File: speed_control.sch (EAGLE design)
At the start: 9 parts

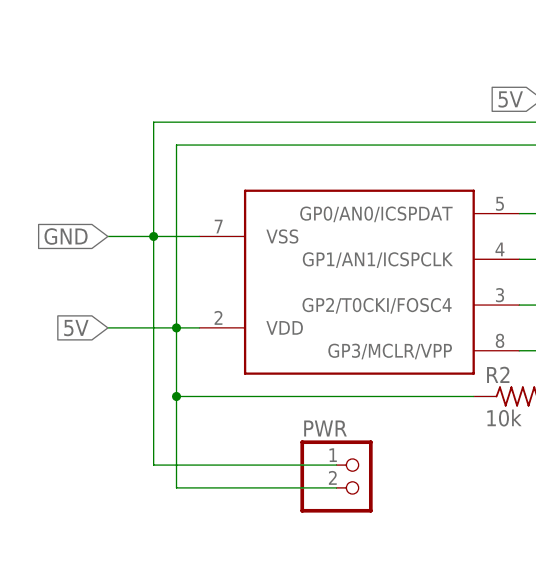
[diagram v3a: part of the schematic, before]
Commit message: Added CAP to circuit
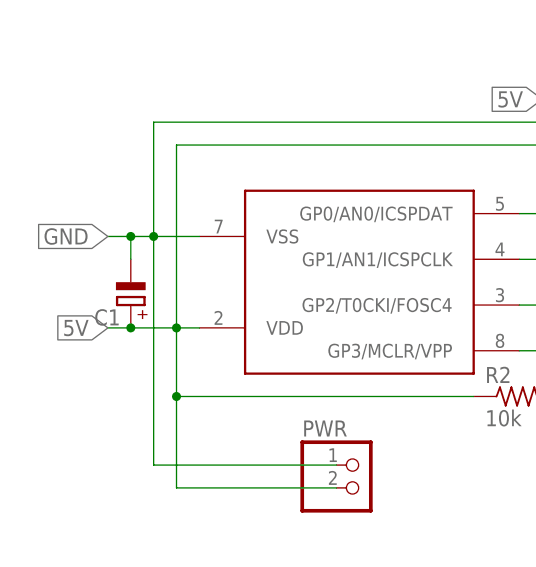
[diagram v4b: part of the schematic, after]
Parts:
- added C1: (no value), rcl:CPOL-EUE3.5-8
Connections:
- net 5V: now also C1.+
- net GND: now also C1.-
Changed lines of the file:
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@@
 <grid distance="0.1" unitdist="inch" unit="inch" style="lines" multiple="1" display="no" altdistance="0.01" altunitdist="inch" altunit="inch"/>
 <layers>
-<layer number="1" name="Top" color="4" fill="1" visible="yes" active="no"/>
-<layer number="2" name="Route2" color="16" fill="1" visible="yes" active="no"/>
-<layer number="3" name="Route3" color="17" fill="1" visible="yes" active="no"/>
-<layer number="4" name="Route4" color="18" fill="1" visible="yes" active="no"/>
-<layer number="5" name="Route5" color="19" fill="1" visible="yes" active="no"/>
-<layer number="6" name="Route6" color="25" fill="1" visible="yes" active="no"/>
-<layer number="7" name="Route7" color="26" fill="1" visible="yes" active="no"/>
-<layer number="8" name="Route8" color="27" fill="1" visible="yes" active="no"/>
-<layer number="9" name="Route9" color="28" fill="1" visible="yes" active="no"/>
-<layer number="10" name="Route10" color="29" fill="1" visible="yes" active="no"/>
-<layer number="11" name="Route11" color="30" fill="1" visible="yes" active="no"/>
-<layer number="12" name="Route12" color="20" fill="1" visible="yes" active="no"/>
-<layer number="13" name="Route13" color="21" fill="1" visible="yes" active="no"/>
-<layer number="14" name="Route14" color="22" fill="1" visible="yes" active="no"/>
-<layer number="15" name="Route15" color="23" fill="1" visible="yes" active="no"/>
-<layer number="16" name="Bottom" color="1" fill="1" visible="yes" active="no"/>
-<layer number="17" name="Pads" color="2" fill="1" visible="yes" active="no"/>
-<layer number="18" name="Vias" color="2" fill="1" visible="yes" active="no"/>
-<layer number="19" name="Unrouted" color="6" fill="1" visible="yes" active="no"/>
-<layer number="20" name="Dimension" color="24" fill="1" visible="yes" active="no"/>
-<layer number="21" name="tPlace" color="7" fill="1" visible="yes" active="no"/>
-<layer number="22" name="bPlace" color="7" fill="1" visible="yes" active="no"/>
-<layer number="23" name="tOrigins" color="15" fill="1" visible="yes" active="no"/>
-<layer number="24" name="bOrigins" color="15" fill="1" visible="yes" active="no"/>
-<layer number="25" name="tNames" color="7" fill="1" visible="yes" active="no"/>
-<layer number="26" name="bNames" color="7" fill="1" visible="yes" active="no"/>
-<layer number="27" name="tValues" color="7" fill="1" visible="yes" active="no"/>
-<layer number="28" name="bValues" color="7" fill="1" visible="yes" active="no"/>
+<layer number="1" name="Top" color="4" fill="1" visible="no" active="no"/>
+<layer number="2" name="Route2" color="16" fill="1" visible="no" active="no"/>
+<layer number="3" name="Route3" color="17" fill="1" visible="no" active="no"/>
+<layer number="4" name="Route4" color="18" fill="1" visible="no" active="no"/>
+<layer number="5" name="Route5" color="19" fill="1" visible="no" active="no"/>
+<layer number="6" name="Route6" color="25" fill="1" visible="no" active="no"/>
+<layer number="7" name="Route7" color="26" fill="1" visible="no" active="no"/>
+<layer number="8" name="Route8" color="27" fill="1" visible="no" active="no"/>
+<layer number="9" name="Route9" color="28" fill="1" visible="no" active="no"/>
+<layer number="10" name="Route10" color="29" fill="1" visible="no" active="no"/>
+<layer number="11" name="Route11" color="30" fill="1" visible="no" active="no"/>
+<layer number="12" name="Route12" color="20" fill="1" visible="no" active="no"/>
+<layer number="13" name="Route13" color="21" fill="1" visible="no" active="no"/>
+<layer number="14" name="Route14" color="22" fill="1" visible="no" active="no"/>
+<layer number="15" name="Route15" color="23" fill="1" visible="no" active="no"/>
+<layer number="16" name="Bottom" color="1" fill="1" visible="no" active="no"/>
+<layer number="17" name="Pads" color="2" fill="1" visible="no" active="no"/>
+<layer number="18" name="Vias" color="2" fill="1" visible="no" active="no"/>
+<layer number="19" name="Unrouted" color="6" fill="1" visible="no" active="no"/>
+<layer number="20" name="Dimension" color="24" fill="1" visible="no" active="no"/>
+<layer number="21" name="tPlace" color="7" fill="1" visible="no" active="no"/>
+<layer number="22" name="bPlace" color="7" fill="1" visible="no" active="no"/>
+<layer number="23" name="tOrigins" color="15" fill="1" visible="no" active="no"/>
+<layer number="24" name="bOrigins" color="15" fill="1" visible="no" active="no"/>
+<layer number="25" name="tNames" color="7" fill="1" visible="no" active="no"/>
+<layer number="26" name="bNames" color="7" fill="1" visible="no" active="no"/>
+<layer number="27" name="tValues" color="7" fill="1" visible="no" active="no"/>
+<layer number="28" name="bValues" color="7" fill="1" visible="no" active="no"/>
 <layer number="29" name="tStop" color="7" fill="3" visible="no" active="no"/>
 <layer number="30" name="bStop" color="7" fill="6" visible="no" active="no"/>
@@
 <layer number="35" name="tGlue" color="7" fill="4" visible="no" active="no"/>
 <layer number="36" name="bGlue" color="7" fill="5" visible="no" active="no"/>
-<layer number="37" name="tTest" color="7" fill="1" visible="yes" active="no"/>
-<layer number="38" name="bTest" color="7" fill="1" visible="yes" active="no"/>
+<layer number="37" name="tTest" color="7" fill="1" visible="no" active="no"/>
+<layer number="38" name="bTest" color="7" fill="1" visible="no" active="no"/>
 <layer number="39" name="tKeepout" color="4" fill="11" visible="no" active="no"/>
 <layer number="40" name="bKeepout" color="1" fill="11" visible="no" active="no"/>
@@
 <layer number="44" name="Drills" color="7" fill="1" visible="no" active="no"/>
 <layer number="45" name="Holes" color="7" fill="1" visible="no" active="no"/>
-<layer number="46" name="Milling" color="3" fill="1" visible="yes" active="no"/>
-<layer number="47" name="Measures" color="7" fill="1" visible="yes" active="no"/>
-<layer number="48" name="Document" color="7" fill="1" visible="yes" active="no"/>
-<layer number="49" name="Reference" color="7" fill="1" visible="yes" active="no"/>
-<layer number="51" name="tDocu" color="7" fill="1" visible="yes" active="no"/>
-<layer number="52" name="bDocu" color="7" fill="1" visible="yes" active="no"/>
+<layer number="46" name="Milling" color="3" fill="1" visible="no" active="no"/>
+<layer number="47" name="Measures" color="7" fill="1" visible="no" active="no"/>
+<layer number="48" name="Document" color="7" fill="1" visible="no" active="no"/>
+<layer number="49" name="Reference" color="7" fill="1" visible="no" active="no"/>
+<layer number="51" name="tDocu" color="7" fill="1" visible="no" active="no"/>
+<layer number="52" name="bDocu" color="7" fill="1" visible="no" active="no"/>
 <layer number="88" name="SimResults" color="9" fill="1" visible="yes" active="yes"/>
 <layer number="89" name="SimProbes" color="9" fill="1" visible="yes" active="yes"/>
@@
 <part name="R3" library="rcl" library_urn="urn:adsk.eagle:library:334" deviceset="R-US_" device="0207/10" package3d_urn="urn:adsk.eagle:package:23491/2" value="1k"/>
 <part name="POT" library="pinhead" library_urn="urn:adsk.eagle:library:325" deviceset="PINHD-1X3" device="" package3d_urn="urn:adsk.eagle:package:22458/2"/>
+<part name="C1" library="rcl" library_urn="urn:adsk.eagle:library:334" deviceset="CPOL-EU" device="E3.5-8" package3d_urn="urn:adsk.eagle:package:23360/2"/>
 </parts>
 <sheets>
@@
 <attribute name="VALUE" x="49.53" y="22.86" size="1.778" layer="96"/>
 </instance>
+<instance part="C1" gate="G$1" x="-27.94" y="-2.54" smashed="yes" rot="R180">
+<attribute name="NAME" x="-29.083" y="-3.0226" size="1.778" layer="95" rot="R180"/>
+<attribute name="VALUE" x="-29.083" y="2.0574" size="1.778" layer="96" rot="R180"/>
+</instance>
 </instances>
 <busses>
@@
 <wire x1="-20.32" y1="5.08" x2="-25.4" y2="5.08" width="0.1524" layer="91"/>
 <label x="-30.48" y="5.08" size="1.778" layer="95" rot="R180" xref="yes"/>
-<wire x1="-25.4" y1="5.08" x2="-30.48" y2="5.08" width="0.1524" layer="91"/>
+<wire x1="-25.4" y1="5.08" x2="-27.94" y2="5.08" width="0.1524" layer="91"/>
 <junction x="-25.4" y="5.08"/>
+<wire x1="-27.94" y1="5.08" x2="-30.48" y2="5.08" width="0.1524" layer="91"/>
 <wire x1="-25.4" y1="-20.32" x2="-25.4" y2="5.08" width="0.1524" layer="91"/>
 <wire x1="-25.4" y1="5.08" x2="-25.4" y2="17.78" width="0.1524" layer="91"/>
@@
 <pinref part="POT" gate="A" pin="1"/>
 <wire x1="20.32" y1="33.02" x2="53.34" y2="33.02" width="0.1524" layer="91"/>
+<pinref part="C1" gate="G$1" pin="-"/>
+<wire x1="-27.94" y1="2.54" x2="-27.94" y2="5.08" width="0.1524" layer="91"/>
+<junction x="-27.94" y="5.08"/>
 </segment>
 <segment>
@@
 <wire x1="-20.32" y1="-5.08" x2="-22.86" y2="-5.08" width="0.1524" layer="91"/>
 <label x="-30.48" y="-5.08" size="1.778" layer="95" rot="R180" xref="yes"/>
-<wire x1="-22.86" y1="-5.08" x2="-30.48" y2="-5.08" width="0.1524" layer="91"/>
+<wire x1="-22.86" y1="-5.08" x2="-27.94" y2="-5.08" width="0.1524" layer="91"/>
+<wire x1="-27.94" y1="-5.08" x2="-30.48" y2="-5.08" width="0.1524" layer="91"/>
 <wire x1="-22.86" y1="-22.86" x2="-22.86" y2="-12.7" width="0.1524" layer="91"/>
 <junction x="-22.86" y="-5.08"/>
@@
 <pinref part="POT" gate="A" pin="3"/>
 <wire x1="53.34" y1="27.94" x2="17.78" y2="27.94" width="0.1524" layer="91"/>
+<pinref part="C1" gate="G$1" pin="+"/>
+<junction x="-27.94" y="-5.08"/>
 </segment>
 <segment>

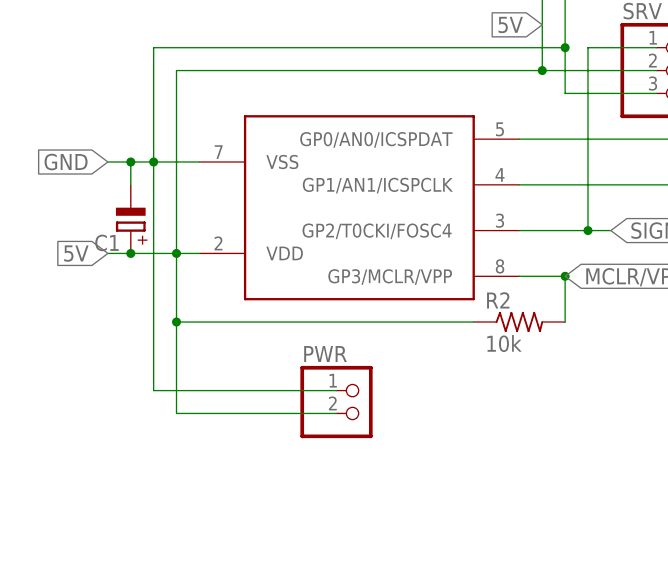
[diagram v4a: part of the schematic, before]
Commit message: Added mounting holes
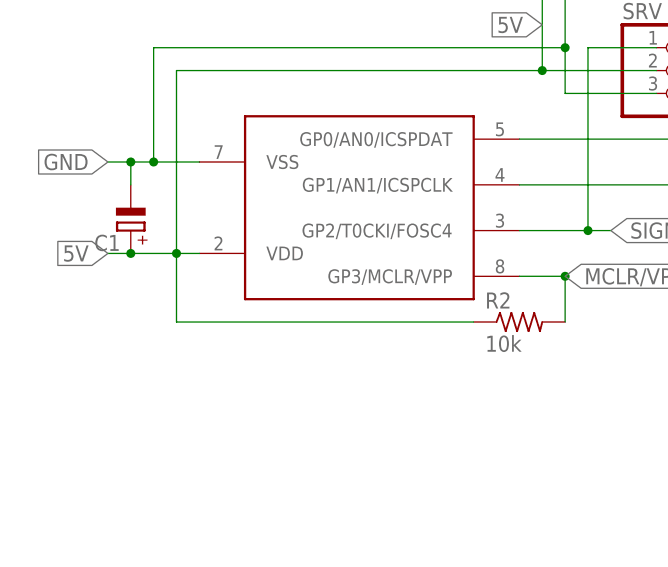
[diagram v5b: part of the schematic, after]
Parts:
- removed PWR: (no value), pinhead:PINHD-1X2/90
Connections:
- net 5V: no longer PWR.2
- net GND: no longer PWR.1
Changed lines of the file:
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@@
 <part name="R1" library="rcl" library_urn="urn:adsk.eagle:library:334" deviceset="R-US_" device="0207/10" package3d_urn="urn:adsk.eagle:package:23491/2" value="270"/>
 <part name="SRV" library="pinhead" library_urn="urn:adsk.eagle:library:325" deviceset="PINHD-1X3" device="/90" package3d_urn="urn:adsk.eagle:package:22459/2"/>
-<part name="PWR" library="pinhead" library_urn="urn:adsk.eagle:library:325" deviceset="PINHD-1X2" device="/90" package3d_urn="urn:adsk.eagle:package:22437/2"/>
 <part name="PRGM" library="pinhead" library_urn="urn:adsk.eagle:library:325" deviceset="PINHD-1X6" device="" package3d_urn="urn:adsk.eagle:package:22472/2"/>
 <part name="U$1" library="PIC10F222" deviceset="PIC10F222" device="PIC10F222" package3d_urn="urn:adsk.eagle:package:16702925/1"/>
@@
 <attribute name="NAME" x="26.67" y="20.955" size="1.778" layer="95"/>
 <attribute name="VALUE" x="26.67" y="7.62" size="1.778" layer="96"/>
-</instance>
-<instance part="PWR" gate="G$1" x="-2.54" y="-22.86" smashed="yes">
-<attribute name="NAME" x="-8.89" y="-17.145" size="1.778" layer="95"/>
-<attribute name="VALUE" x="-8.89" y="-27.94" size="1.778" layer="96"/>
 </instance>
 <instance part="PRGM" gate="A" x="96.52" y="17.78" smashed="yes">
@@
 <junction x="-25.4" y="5.08"/>
 <wire x1="-27.94" y1="5.08" x2="-30.48" y2="5.08" width="0.1524" layer="91"/>
-<wire x1="-25.4" y1="-20.32" x2="-25.4" y2="5.08" width="0.1524" layer="91"/>
 <wire x1="-25.4" y1="5.08" x2="-25.4" y2="17.78" width="0.1524" layer="91"/>
 <wire x1="-25.4" y1="17.78" x2="20.32" y2="17.78" width="0.1524" layer="91"/>
 <pinref part="U$1" gate="G$1" pin="VSS"/>
-<pinref part="PWR" gate="G$1" pin="1"/>
 <wire x1="20.32" y1="33.02" x2="20.32" y2="17.78" width="0.1524" layer="91"/>
-<wire x1="-5.08" y1="-20.32" x2="-25.4" y2="-20.32" width="0.1524" layer="91"/>
 <wire x1="20.32" y1="17.78" x2="20.32" y2="12.7" width="0.1524" layer="91"/>
 <junction x="20.32" y="17.78"/>
@@
 <wire x1="-22.86" y1="-5.08" x2="-27.94" y2="-5.08" width="0.1524" layer="91"/>
 <wire x1="-27.94" y1="-5.08" x2="-30.48" y2="-5.08" width="0.1524" layer="91"/>
-<wire x1="-22.86" y1="-22.86" x2="-22.86" y2="-12.7" width="0.1524" layer="91"/>
 <junction x="-22.86" y="-5.08"/>
 <wire x1="-22.86" y1="-12.7" x2="-22.86" y2="-5.08" width="0.1524" layer="91"/>
@@
 <wire x1="17.78" y1="15.24" x2="30.48" y2="15.24" width="0.1524" layer="91"/>
 <wire x1="-22.86" y1="-12.7" x2="10.16" y2="-12.7" width="0.1524" layer="91"/>
-<junction x="-22.86" y="-12.7"/>
 <pinref part="R2" gate="G$1" pin="1"/>
 <junction x="17.78" y="15.24"/>
-<pinref part="PWR" gate="G$1" pin="2"/>
 <wire x1="17.78" y1="27.94" x2="17.78" y2="15.24" width="0.1524" layer="91"/>
-<wire x1="-22.86" y1="-22.86" x2="-5.08" y2="-22.86" width="0.1524" layer="91"/>
 <label x="17.78" y="20.32" size="1.778" layer="95" rot="R180" xref="yes"/>
 <pinref part="POT" gate="A" pin="3"/>
